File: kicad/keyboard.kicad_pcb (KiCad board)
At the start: 2 copper layers, 224.7 x 91.7 mm, 121 parts, among them SW1 SW_MX, SW10 SW_MX, SW11 SW_MX, SW12 SW_MX, SW13 SW_MX, SW14 SW_MX, SW15 SW_MX, SW16 SW_MX, SW17 SW_MX, SW18 SW_MX, SW19 SW_MX, SW2 SW_MX, SW20 SW_MX, SW21 SW_MX, SW22 SW_MX, SW23 SW_MX, SW24 SW_MX, SW25 SW_MX, SW26 SW_MX, SW27 SW_MX, SW28 SW_MX, SW29 SW_MX, SW3 SW_MX, SW30 SW_MX, SW31 SW_MX, SW32 SW_MX, SW33 SW_MX, SW34 SW_MX, SW35 SW_MX, SW36 SW_MX, SW37 SW_MX, SW38 SW_MX, SW39 SW_MX, SW4 SW_MX, SW40 SW_MX, SW41 SW_MX, SW42 SW_MX, SW43 SW_MX, SW44 SW_MX, SW45 SW_MX, SW46 SW_MX, SW47 SW_MX, SW48 SW_MX, SW49 SW_MX, SW5 SW_MX, SW50 SW_MX, SW51 SW_MX, SW52 SW_MX, SW53 SW_MX, SW54 SW_MX, SW55 SW_MX, SW56 SW_MX, SW57 SW_MX, SW58 SW_MX, SW59 SW_MX, SW6 SW_MX, SW60 SW_MX, SW7 SW_MX, SW8 SW_MX, SW9 SW_MX

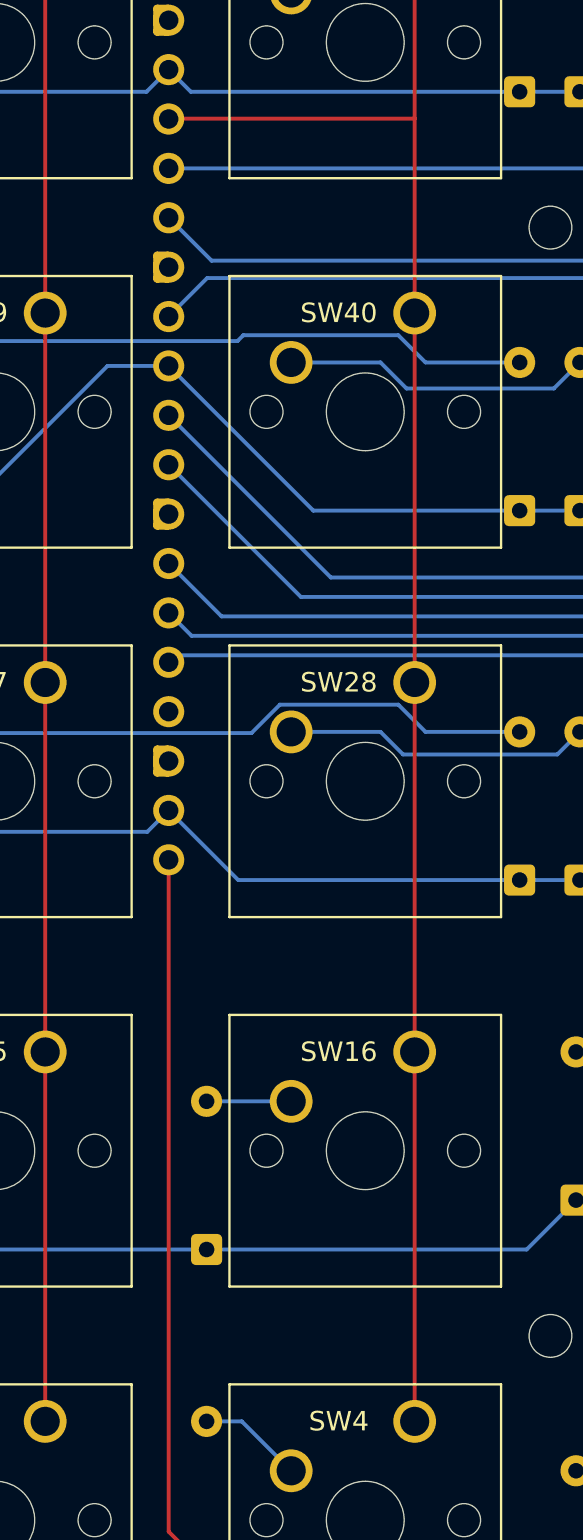
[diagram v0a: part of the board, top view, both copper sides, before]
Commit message: Reroute trace
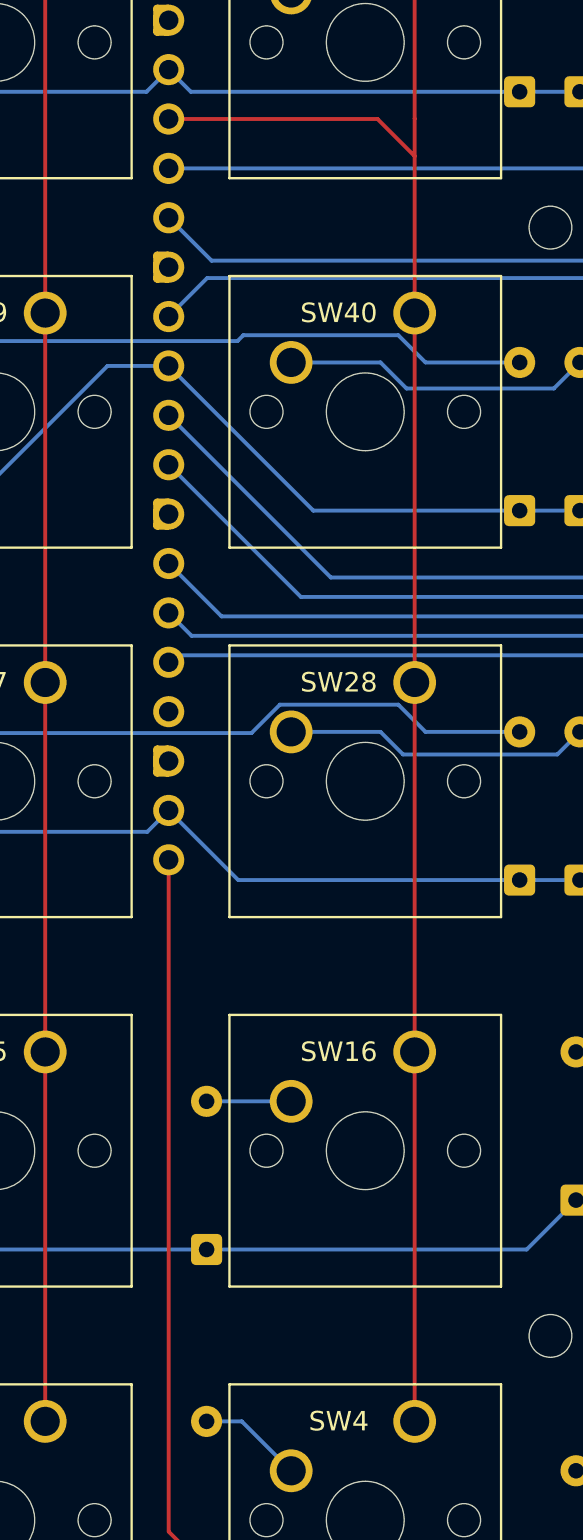
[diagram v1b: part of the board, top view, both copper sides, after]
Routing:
- net COL3: track 88.7 -> 89.5 mm
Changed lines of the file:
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@@
+	)
+	(segment
+		(start 103.09 60.52)
+		(end 105 62.43)
+		(width 0.2)
+		(layer "F.Cu")
+		(net "COL3")
+	)
+	(segment
+		(start 92.35 60.52)
+		(end 103.09 60.52)
+		(width 0.2)
+		(layer "F.Cu")
+		(net "COL3")
 	)
 	(segment
@@
 	)
 	(segment
-		(start 92.37 60.5)
-		(end 105 60.5)
+		(start 105 60.5)
+		(end 105 62.43)
 		(width 0.2)
 		(layer "F.Cu")
@@
 	)
 	(segment
-		(start 105 60.5)
+		(start 105 62.43)
 		(end 105 127.5)
 		(width 0.2)
